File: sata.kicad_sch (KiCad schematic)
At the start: 18 parts, among them J4 SATA_Backplane, U1 NCP45521, U2 NCP45521

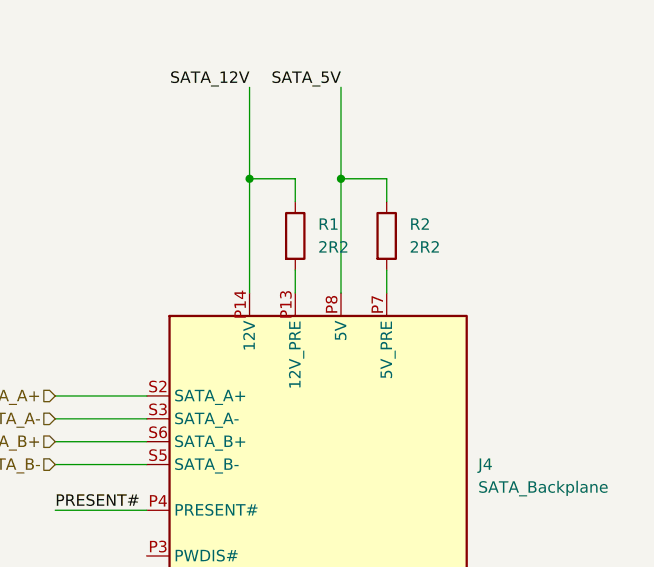
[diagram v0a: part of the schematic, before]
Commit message: Routing power
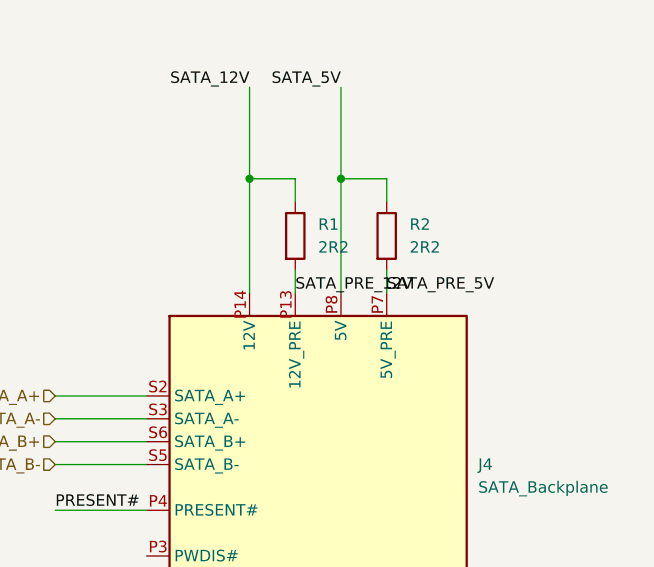
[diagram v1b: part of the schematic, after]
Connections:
- net SATA_PRE_12V: now reaches J4.P13 (12V_PRE), R1.2
- net SATA_PRE_5V: now reaches J4.P7 (5V_PRE), R2.2
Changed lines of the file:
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@@
+    (effects (font (size 1.27 1.27)) (justify left bottom))
+  )
+  (label "SATA_PRE_12V" (at 217.17 60.96 0) (fields_autoplaced)
     (effects (font (size 1.27 1.27)) (justify left bottom))
   )
@@
     (effects (font (size 1.27 1.27)) (justify right bottom))
   )
+  (label "SATA_PRE_5V" (at 227.33 60.96 0) (fields_autoplaced)
+    (effects (font (size 1.27 1.27)) (justify left bottom))
+  )
   (label "SATA_5V" (at 80.01 43.18 180) (fields_autoplaced)

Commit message: Finish v1.0
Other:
- note added: "SATA connector with power circuitry"
- note added: "The power circuit I reverse engineered on the existing backplane PCB ended up being a discreet load switch for each power rail (5V and 12V, per drive) with a slow starter. Pin P4 on the SATA connector is used as a detect pin as it's shorted to ground when a drive is connected, enabling the load switch. Instead of re-creating this discrete circuit I used NCP45521-L to handle this for me. The defau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"
- title: (none) -> F3 Backplane SATA
- moved on the sheet: C10, C11, C12, C13, C14, C15, C16, C17, C18, C19, C20, C21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

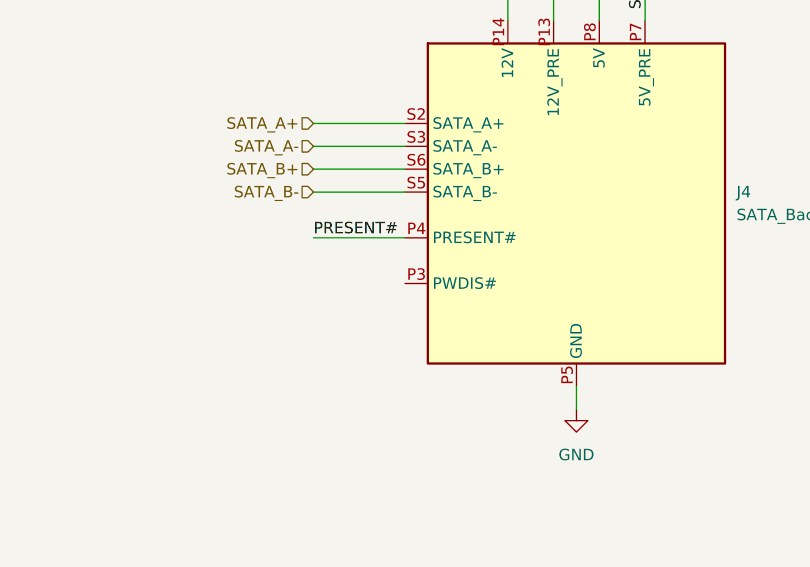
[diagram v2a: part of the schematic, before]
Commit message: Add datasheet links and digikey part numbers
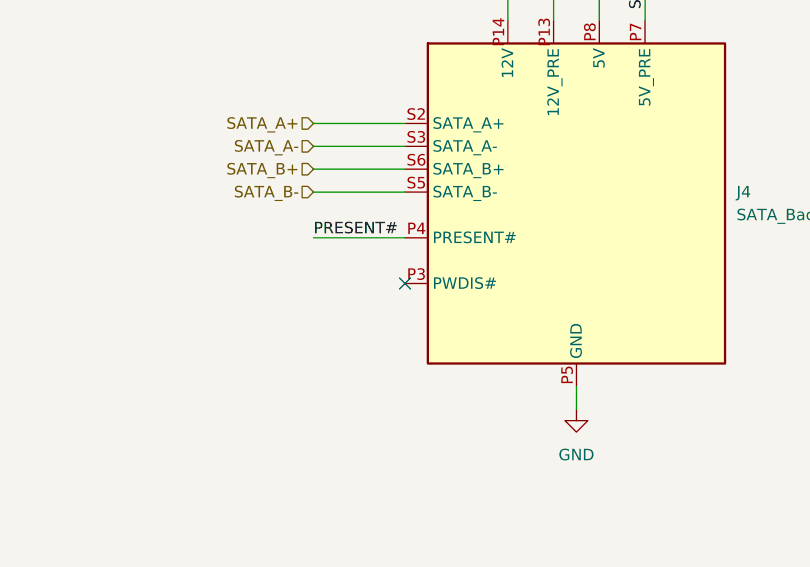
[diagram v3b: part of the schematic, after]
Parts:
- J4: Digikey Part No. (none) -> WM3587-ND
- U1, U2: Digikey Part No. (none) -> NCP45521IMNTWG-LOSCT-ND
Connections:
- no-connect marks 2 -> 3
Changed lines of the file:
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@@
   )
   (no_connect (at 71.12 166.37))
+  (no_connect (at 205.74 118.11))
   (no_connect (at 71.12 90.17))
   (wire (pts (xy 88.9 158.75) (xy 101.6 158.75))
@@
       (effects (font (size 1.27 1.27)) hide)
     )
-    (property "Datasheet" "" (at 48.26 146.05 0)
+    (property "Datasheet" "https://www.onsemi.com/pdf/datasheet/ncp45520-d.pdf" (at 48.26 146.05 0)
+      (effects (font (size 1.27 1.27)) hide)
+    )
+    (property "Digikey Part No." "NCP45521IMNTWG-LOSCT-ND" (at 59.69 162.56 0)
       (effects (font (size 1.27 1.27)) hide)
     )
@@
       (effects (font (size 1.27 1.27)) hide)
     )
-    (property "Datasheet" "" (at 48.26 69.85 0)
+    (property "Datasheet" "https://www.onsemi.com/pdf/datasheet/ncp45520-d.pdf" (at 48.26 69.85 0)
+      (effects (font (size 1.27 1.27)) hide)
+    )
+    (property "Digikey Part No." "NCP45521IMNTWG-LOSCT-ND" (at 59.69 86.36 0)
       (effects (font (size 1.27 1.27)) hide)
     )
@@
       (effects (font (size 1.27 1.27)) hide)
     )
-    (property "Datasheet" "" (at 224.79 99.06 0)
-      (effects (font (size 1.27 1.27)) hide)
-    )
+    (property "Datasheet" "https://www.molex.com/content/dam/molex/molex-dot-com/products/automated/en-us/salesdrawingpdf/877/87701/877011001_sd.pdf" (at 224.79 99.06 0)
+      (effects (font (size 1.27 1.27)) hide)
+    )
+    (property "Digikey Part No." "WM3587-ND" (at 224.79 109.22 0)
+      (effects (font (size 1.27 1.27)) hide)
+    )
